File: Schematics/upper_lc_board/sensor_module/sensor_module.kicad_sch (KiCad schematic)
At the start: 54 parts, among them J2 HAL_SENS, J3 PT1, J4 PT2, J7 TC, U10 OA-TLV9001IDCK, U11 OA-TLV9001IDCK, U12 OA-TLV9001IDCK, U5 TMP117MAIDRVR, U7 ADC_ADS131M04IPWR, U9 OA-TLV9001IDCK

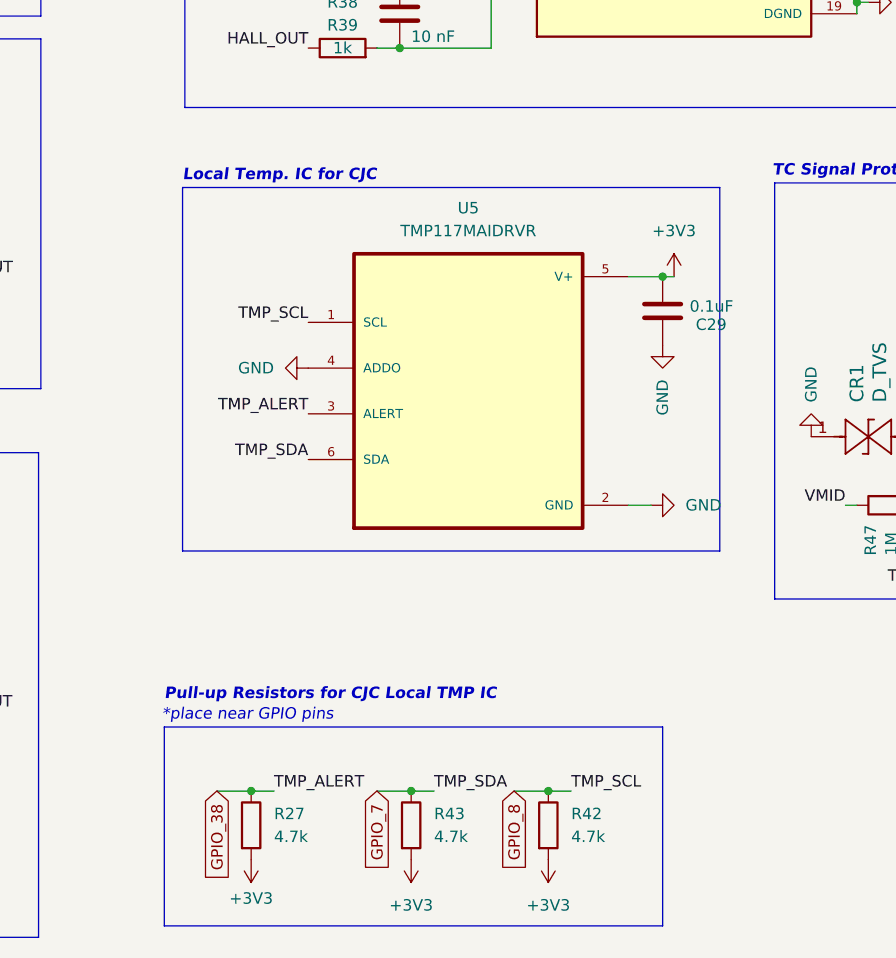
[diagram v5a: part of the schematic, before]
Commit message: add thermistor circuitry & update layout
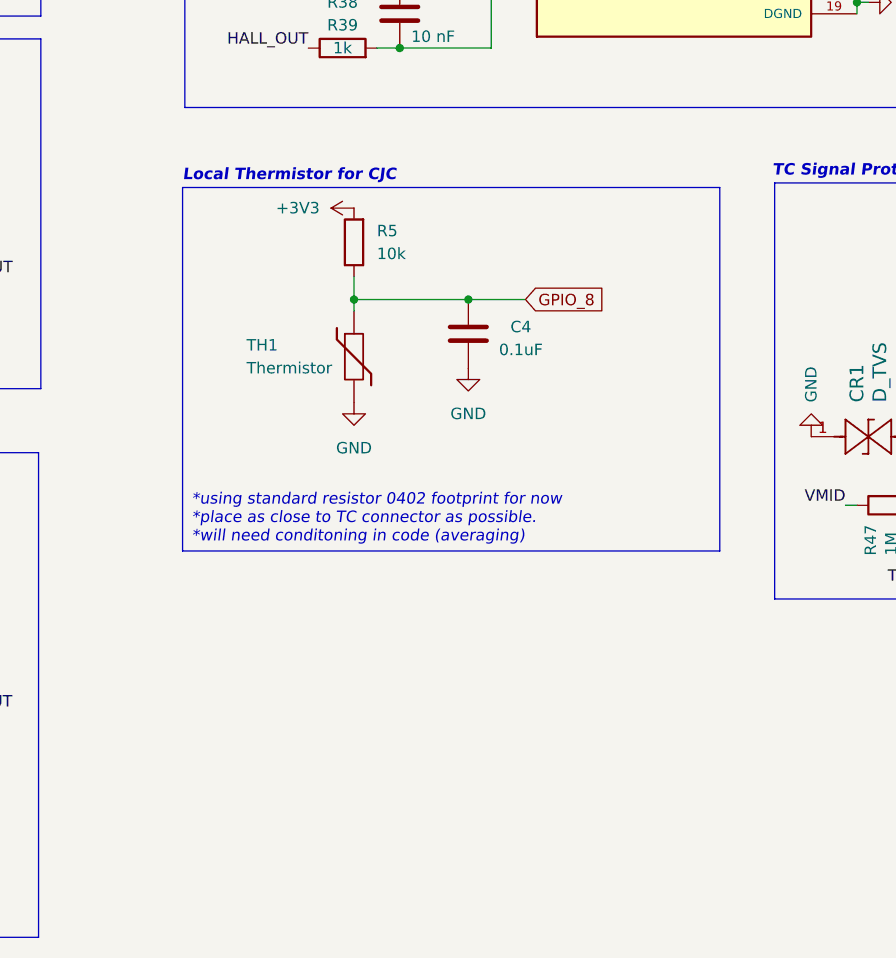
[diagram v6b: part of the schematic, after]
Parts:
- removed C29: 0.1uF, Capacitor_SMD:C_0603_1608Metric, symbol Device:C
- removed R27, R42, R43: 4.7k, Resistor_SMD:R_0402_1005Metric, symbol Device:R
- removed U5: TMP117MAIDRVR, TMP117MAIDRVR:SON65P200X200X80-7N, symbol TMP117MAIDRVR:TMP117MAIDRVR
- added C4: 0.1uF, Capacitor_SMD:C_0603_1608Metric, symbol Device:C
- added R5: 10k, Resistor_SMD:R_0402_1005Metric, symbol Device:R
- added TH1: Thermistor, Resistor_SMD:R_0402_1005Metric, symbol Device:Thermistor
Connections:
- net +3V3: now also R5.2
- net GND: now also C4.1, TH1.2
- net GPIO_8: now also C4.2, R5.1, TH1.1
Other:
- note added: "*using standard resistor 0402 footprint for now *place as close to TC connector as possible. *will need conditoning in code (averaging)"
- note added: "Local Thermistor for CJC"
- note removed: "*place near GPIO pins"
- note removed: "Local Temp. IC for CJC"
- note removed: "Pull-up Resistors for CJC Local TMP IC"

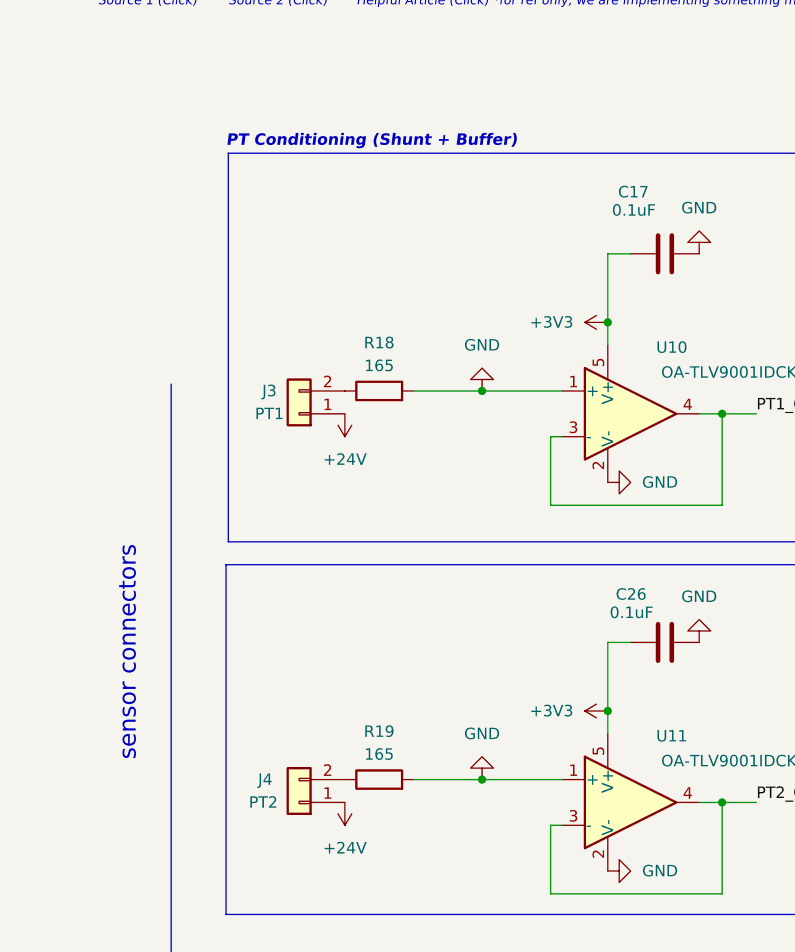
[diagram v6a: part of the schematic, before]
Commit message: fix shunt resistor, add test point to layout
- sync issue with backplane connector footprint
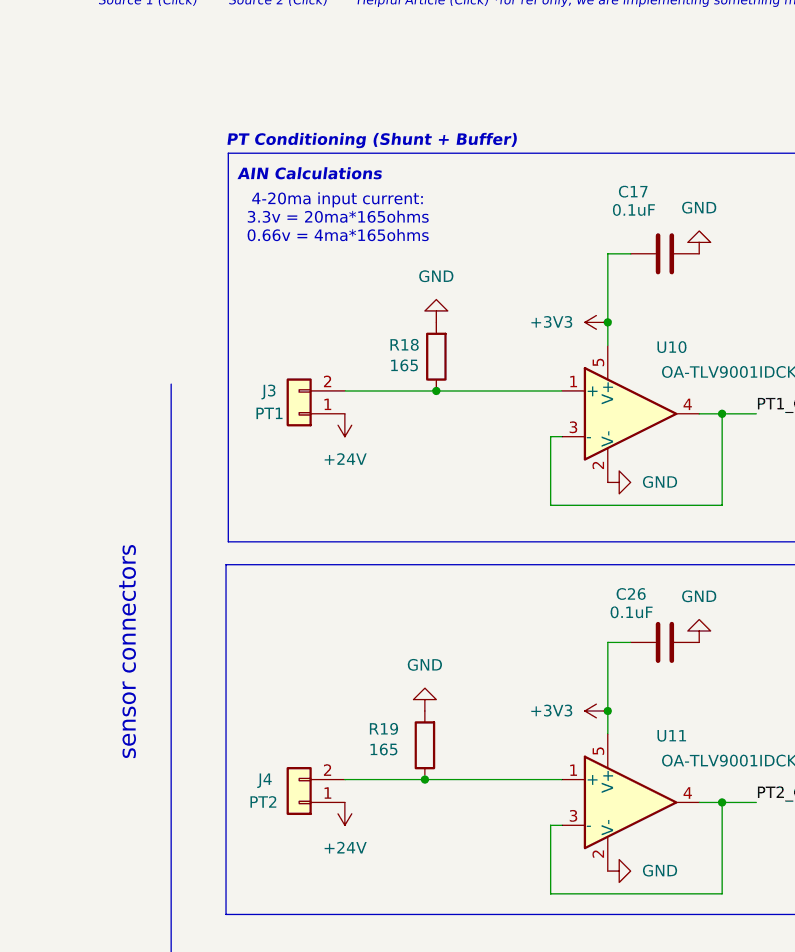
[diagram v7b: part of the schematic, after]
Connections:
- net GND: no longer U10.1 (+), U11.1 (+)
- net at J4.2 (Pin_2), R19.1: now also U11.1 (+)
- net at J3.2 (Pin_2), R18.1: now also U10.1 (+)
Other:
- note added: "4-20ma input current: 3.3v = 20ma*165ohms 0.66v = 4ma*165ohms"
- note added: "AIN Calculations"
- moved on the sheet: R18, R19

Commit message: routing work
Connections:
- net GPIO_11 is gone; now on net GPIO_48: U7.15 (DOUT)
- net GPIO_10: now also U7.14 (SCLK); no longer U7.13 (~{DRDY})
- net GPIO_15: now also U7.17 (CLKIN); no longer R31.1
- net GPIO_48: no longer U7.17 (CLKIN)
- net GPIO_9: now also U7.13 (~{DRDY}); no longer U7.14 (SCLK)
- net GPIO_12 renamed GPIO_38
- net GPIO_16 renamed GPIO_47
- new net GPIO_40: R31.1
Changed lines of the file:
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@@
+		)
+	)
+	(global_label "GPIO_40"
+		(shape input)
+		(at 233.68 62.23 90)
+		(fields_autoplaced yes)
+		(effects
+			(font
+				(size 1.27 1.27)
+			)
+			(justify left)
+		)
+		(property "Intersheetrefs" "${INTERSHEET_REFS}"
+			(at 233.68 51.3829 90)
+			(effects
+				(font
+					(size 1.27 1.27)
+				)
+				(justify left)
+				(hide yes)
+			)
+		)
+	)
+	(global_label "GPIO_10"
+		(shape input)
+		(at 191.77 67.31 0)
+		(fields_autoplaced yes)
+		(effects
+			(font
+				(size 1.27 1.27)
+			)
+			(justify left)
+		)
+		(property "Intersheetrefs" "${INTERSHEET_REFS}"
+			(at 202.6171 67.31 0)
+			(effects
+				(font
+					(size 1.27 1.27)
+				)
+				(justify left)
+				(hide yes)
+			)
+		)
+	)
+	(global_label "GPIO_9"
+		(shape input)
+		(at 191.77 74.93 0)
+		(fields_autoplaced yes)
+		(effects
+			(font
+				(size 1.27 1.27)
+			)
+			(justify left)
+		)
+		(property "Intersheetrefs" "${INTERSHEET_REFS}"
+			(at 201.4076 74.93 0)
+			(effects
+				(font
+					(size 1.27 1.27)
+				)
+				(justify left)
+				(hide yes)
+			)
 		)
 	)
@@
 		)
 	)
-	(global_label "GPIO_9"
-		(shape input)
-		(at 191.77 67.31 0)
-		(fields_autoplaced yes)
-		(effects
-			(font
-				(size 1.27 1.27)
-			)
-			(justify left)
-		)
-		(property "Intersheetrefs" "${INTERSHEET_REFS}"
-			(at 201.4076 67.31 0)
+	(global_label "GPIO_38"
+		(shape input)
+		(at 266.7 62.23 90)
+		(fields_autoplaced yes)
+		(effects
+			(font
+				(size 1.27 1.27)
+			)
+			(justify left)
+		)
+		(property "Intersheetrefs" "${INTERSHEET_REFS}"
+			(at 266.7 51.3829 90)
+			(effects
+				(font
+					(size 1.27 1.27)
+				)
+				(justify left)
+				(hide yes)
+			)
+		)
+	)
+	(global_label "GPIO_47"
+		(shape input)
+		(at 191.77 69.85 0)
+		(fields_autoplaced yes)
+		(effects
+			(font
+				(size 1.27 1.27)
+			)
+			(justify left)
+		)
+		(property "Intersheetrefs" "${INTERSHEET_REFS}"
+			(at 202.6171 69.85 0)
 			(effects
 				(font
@@
 		)
 	)
-	(global_label "GPIO_10"
-		(shape input)
-		(at 191.77 74.93 0)
-		(fields_autoplaced yes)
-		(effects
-			(font
-				(size 1.27 1.27)
-			)
-			(justify left)
-		)
-		(property "Intersheetrefs" "${INTERSHEET_REFS}"
-			(at 202.6171 74.93 0)
+	(global_label "GPIO_15"
+		(shape input)
+		(at 191.77 59.69 0)
+		(fields_autoplaced yes)
+		(effects
+			(font
+				(size 1.27 1.27)
+			)
+			(justify left)
+		)
+		(property "Intersheetrefs" "${INTERSHEET_REFS}"
+			(at 202.6171 59.69 0)
 			(effects
 				(font
@@
 	(global_label "GPIO_48"
 		(shape input)
-		(at 191.77 59.69 0)
-		(fields_autoplaced yes)
-		(effects
-			(font
-				(size 1.27 1.27)
-			)
-			(justify left)
-		)
-		(property "Intersheetrefs" "${INTERSHEET_REFS}"
-			(at 202.6171 59.69 0)
-			(effects
-				(font
-					(size 1.27 1.27)
-				)
-				(justify left)
-				(hide yes)
-			)
-		)
-	)
-	(global_label "GPIO_16"
-		(shape input)
-		(at 191.77 69.85 0)
-		(fields_autoplaced yes)
-		(effects
-			(font
-				(size 1.27 1.27)
-			)
-			(justify left)
-		)
-		(property "Intersheetrefs" "${INTERSHEET_REFS}"
-			(at 202.6171 69.85 0)
-			(effects
-				(font
-					(size 1.27 1.27)
-				)
-				(justify left)
-				(hide yes)
-			)
-		)
-	)
-	(global_label "GPIO_15"
-		(shape input)
-		(at 233.68 62.23 90)
-		(fields_autoplaced yes)
-		(effects
-			(font
-				(size 1.27 1.27)
-			)
-			(justify left)
-		)
-		(property "Intersheetrefs" "${INTERSHEET_REFS}"
-			(at 233.68 51.3829 90)
-			(effects
-				(font
-					(size 1.27 1.27)
-				)
-				(justify left)
-				(hide yes)
-			)
-		)
-	)
-	(global_label "GPIO_11"
-		(shape input)
 		(at 191.77 72.39 0)
 		(fields_autoplaced yes)
@@
 			(effects
 				(font
-					(size 1.27 1.27)
-				)
-				(justify left)
-				(hide yes)
-			)
-		)
-	)
-	(global_label "GPIO_12"
-		(shape input)
-		(at 266.7 62.23 90)
-		(fields_autoplaced yes)
-		(effects
-			(font
-				(size 1.27 1.27)
-			)
-			(justify left)
-		)
-		(property "Intersheetrefs" "${INTERSHEET_REFS}"
-			(at 266.7 51.3829 90)
-			(effects
-				(font
